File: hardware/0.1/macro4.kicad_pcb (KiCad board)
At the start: 2 copper layers, 48 x 48 mm, 24 parts, among them J1 USB_C_Receptacle_USB2.0, SW1 DFU, SW2 RST, SW3 SW_Push, SW5 SW_Push, SW6 SW_Push, SW7 Rotary_Encoder_MX, U1 AP2112K-3.3, U2 STM32F072C8Tx

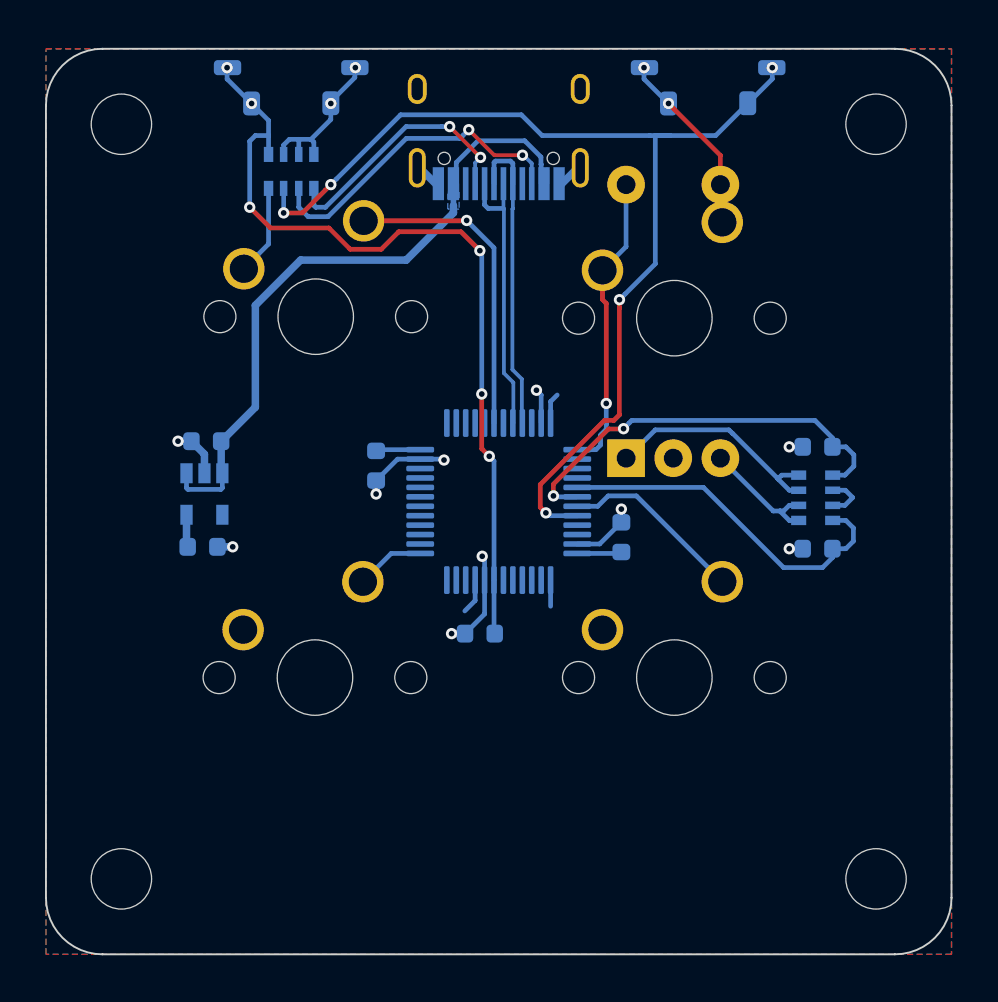
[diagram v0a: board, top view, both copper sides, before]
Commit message: add RGB and silk to macro4
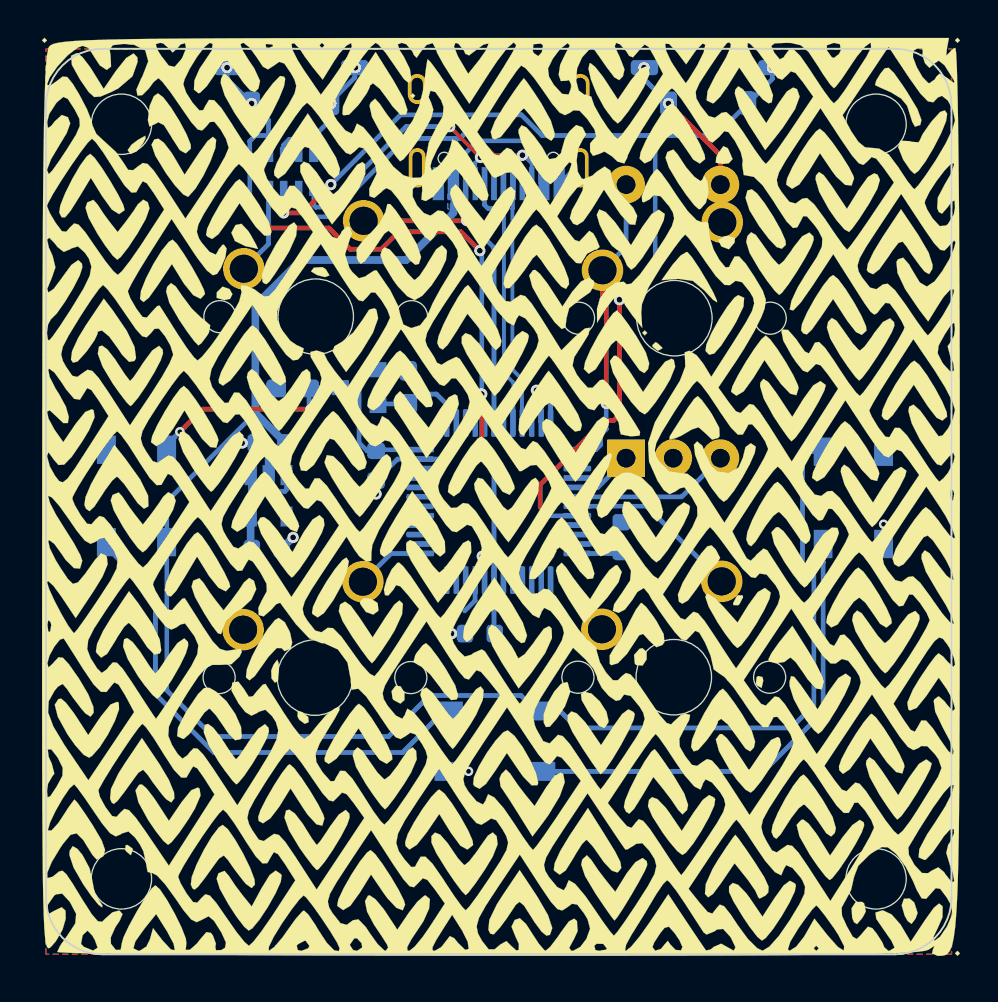
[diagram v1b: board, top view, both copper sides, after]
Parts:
- removed C6, C7: 100n, Capacitor_SMD:C_0603_1608Metric
- removed RN2: 10K, Resistor_SMD:R_Array_Convex_4x0603
- added D1: WS2812B, LED_SMD:LED_WS2812B_PLCC4_5.0x5.0mm_P3.2mm, B.Cu at (58.8, 111.7)
- added D2: WS2812B, LED_SMD:LED_WS2812B_PLCC4_5.0x5.0mm_P3.2mm, B.Cu at (77.8, 124.7)
- added D3: WS2812B, LED_SMD:LED_WS2812B_PLCC4_5.0x5.0mm_P3.2mm, B.Cu at (96.8, 111.8)
- added G***: LOGO, art:pattern_back, F.Cu at (78.2, 111.7)
- added G***: LOGO, art:pattern_top, F.Cu at (78.1, 111.8)
- added Q1: BSS138, Package_TO_SOT_SMD:SOT-23, B.Cu at (70.6, 106.0)
- added R1: 10K, Resistor_SMD:R_0603_1608Metric_Pad1.05x0.95mm_HandSolder, B.Cu at (73.2, 106.0)
- added R2: 10K, Resistor_SMD:R_0603_1608Metric_Pad1.05x0.95mm_HandSolder, B.Cu at (67.1, 106.0)
- SW3, SW5, SW6: value SW_Push -> CHERRY_MX
- moved C1 3.40 mm to (65.9, 108.9)
- moved C3 3.40 mm to (65.7, 114.5)
- moved U1 3.40 mm to (65.8, 111.7)
- moved G*** 0.28 mm to (77.7, 129.9)
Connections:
- SW7 pad A: Net-(RN2-Pad3) -> /ENC_A
- SW7 pad B: Net-(RN2-Pad1) -> /ENC_B
- U2 pad 25: (no net) -> /LED
- U2 pad 41: /ENC_B -> /ENC_A
- U2 pad 42: /ENC_A -> /ENC_B
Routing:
- net VBUS: track 36.6 -> 106.4 mm
- net Net-(D1-Pad2): track 0.00 -> 26.9 mm
- net Net-(D2-Pad2): track 0.00 -> 25.1 mm
- net /ENC_A: track 22.2 -> 3.26 mm, vias 2 -> 0
- net Net-(RN2-Pad3): track 12.3 -> 0.00 mm
- net Net-(D1-Pad4): track 0.00 -> 11.4 mm, vias 0 -> 2
- net /ENC_B: track 19.2 -> 8.44 mm
- net Net-(RN2-Pad1): track 6.64 -> 0.00 mm
- net /LED: track 0.00 -> 5.12 mm
- net +3V3: track 28.5 -> 33.5 mm
- net GND: track 32.3 -> 34.0 mm, vias 12 -> 13

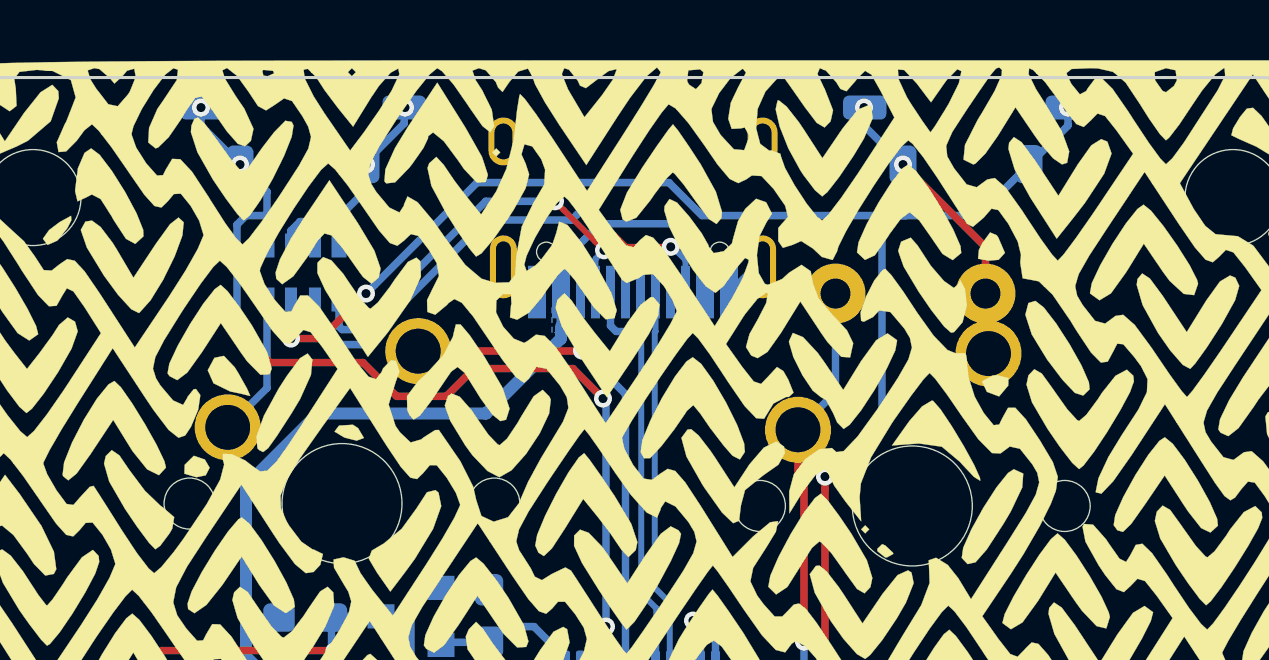
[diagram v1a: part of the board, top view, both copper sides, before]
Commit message: change buttons
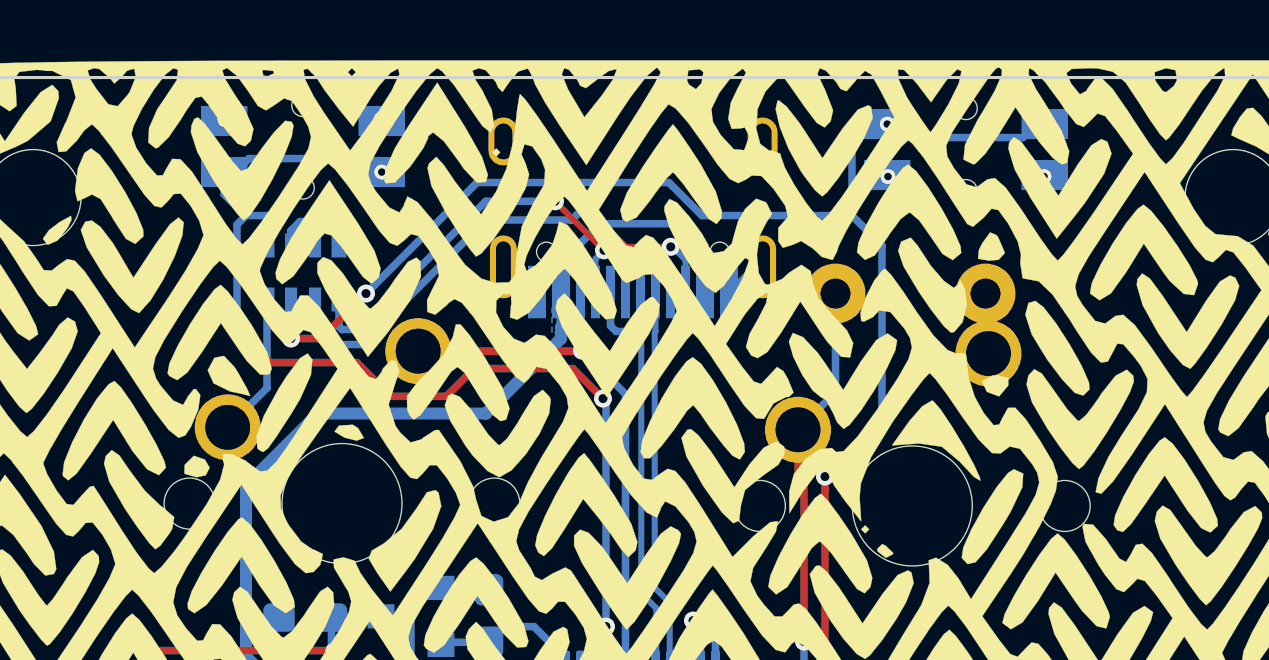
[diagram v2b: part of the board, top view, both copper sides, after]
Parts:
- removed the G*** at (78.2, 111.7)
- SW1, SW2: footprint josh-buttons-switches:TL3330AF130QG -> josh-buttons-switches:Panasonic_EVQPUL_EVQPUC
- moved SW1 0.40 mm to (89.1, 90.4), turned to 180 degrees
- moved SW2 0.30 mm to (67.0, 90.3), turned to 180 degrees
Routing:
- net +3V3: track 33.5 -> 25.6 mm
- net GND: track 34.0 -> 29.4 mm, vias 13 -> 14
- net /nRST: track 44.7 -> 47.8 mm
- net /BOOT0: track 57.1 -> 57.5 mm, vias 5 -> 6

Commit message: update due to breaking lib change
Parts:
- removed G***: LOGO, art:pattern_top
- removed G***: LOGO, josh-logos:josh-johnson-logo-17x3
- removed REF**: Josh Details, josh-logos:josh-details
- added LOGO1: Josh-Logo, josh-logos:josh-johnson-logo-11x2, B.Cu at (79.2, 130.8)
- added LOGO2: Josh-Details, josh-logos:josh-details, B.Cu at (80.1, 132.0)
- added LOGO3: OSHW Logo, josh-logos:OSHW_Logo_3.6x3.6_F.Mask, B.Cu at (68.8, 131.5)
- added LOGO4: F-Silk-Art, art:pattern_top, F.Cu at (77.9, 112.2)
- J1: footprint josh-connectors:USB_C_Receptacle_GT-USB-7010 -> josh-connectors:USB_C_U262-161N-4BVC11
- SW1, SW2: footprint josh-buttons-switches:Panasonic_EVQPUL_EVQPUC -> josh-buttons-switches:SW_Push_EVQPUL_EVQPUC
- SW3, SW5, SW6: footprint josh-buttons-switches:SW_Cherry_MX_1.00u_PCB -> josh-keyboard:MX_KEYSWITCH
- SW7: footprint josh-buttons-switches:MX_KEYSWITCH_ENCODER -> josh-keyboard:MX_KEYSWITCH_ENCODER
- moved SW6 5.72 mm to (68.3, 102.2)
- moved SW3 5.68 mm to (87.3, 121.3)
- moved SW5 5.63 mm to (68.3, 121.3)

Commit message: v0.2
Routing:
- net +3V3: track 25.6 -> 30.4 mm
